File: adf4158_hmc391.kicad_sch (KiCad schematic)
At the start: 48 parts, among them U4 HMC391, U5 AD8065, U6 ADF4158, Y1 KT2016K

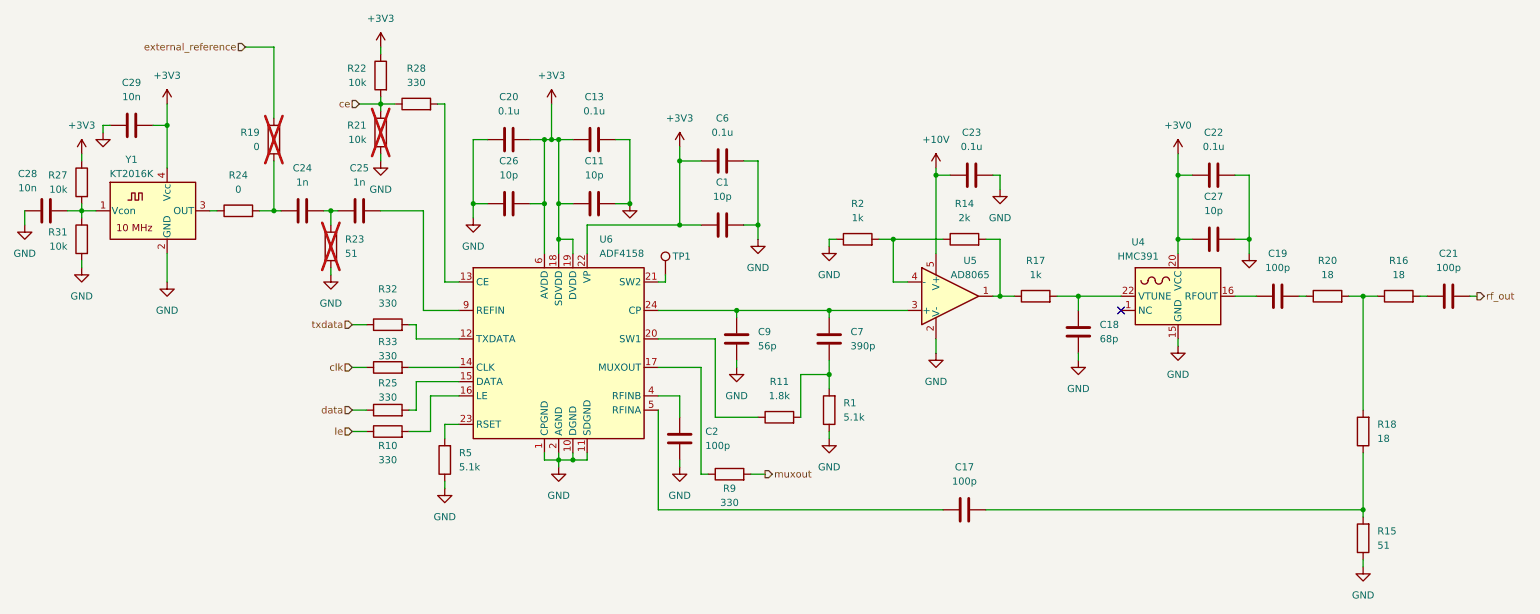
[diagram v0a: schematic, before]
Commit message: switch to 4-layer 1.6mm PCB stackup from JLCPCB
- By recommendation of reviewers, use a 4-layer 1.6 PCB stackup from
JLCPCB that gives 0.6 mm 50 ohm CPWG traces on the top layer.

- Use an SMA connector with a thin pin for the RF output.

- Remove 51 ohm resistor loading the ADF4518 PCB. This is believed
to be a mistake in the evaluation board schematic.

- Add M2 mounting holes to the board corners.

- Connect NC pins of HMC391 to GND as in the evaluation board.

Signed-off-by: Daniel Estévez <daniel@destevez.net>
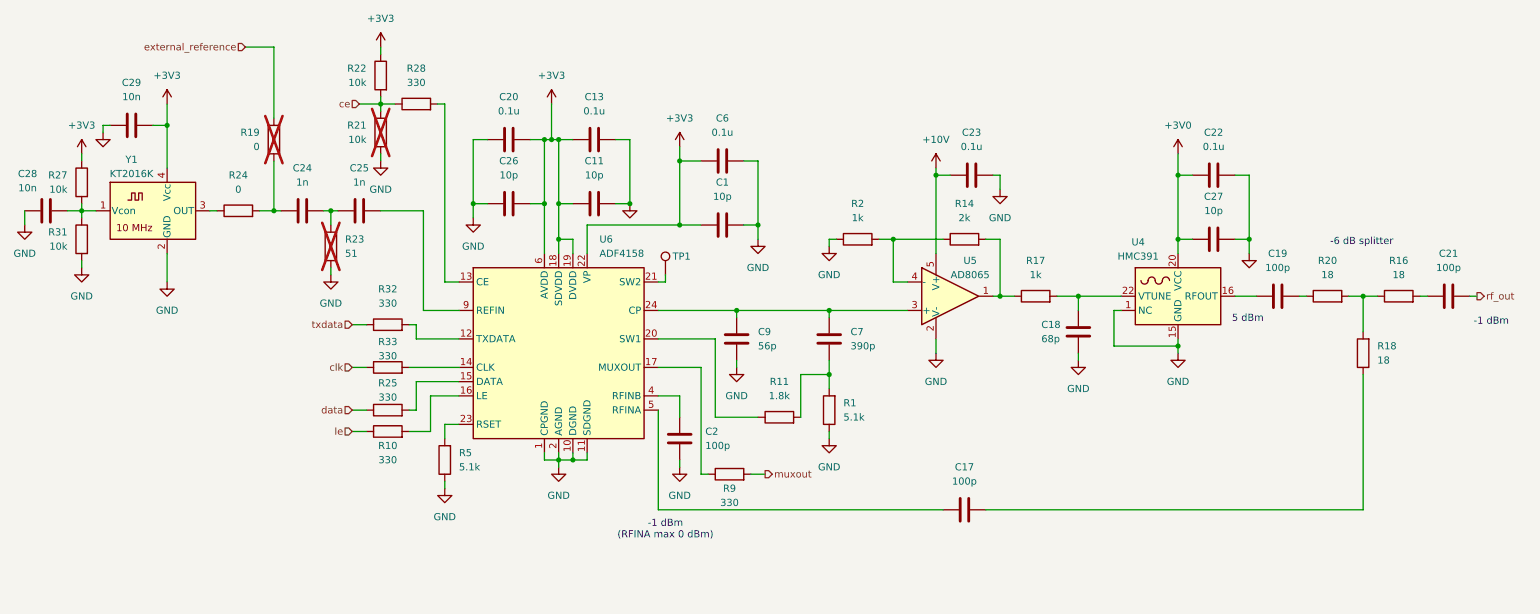
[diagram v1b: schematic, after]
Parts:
- removed R15: 51, Resistor_SMD:R_0402_1005Metric, symbol Device:R
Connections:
- net GND: now also U4.1 (NC), U4.10 (NC), U4.11 (NC), U4.12 (NC), U4.13 (NC), U4.14 (NC), U4.17 (NC), U4.18 (NC), U4.19 (NC), U4.2 (NC), U4.21 (NC), U4.23 (NC), U4.24 (NC), U4.3 (NC), U4.4 (NC), U4.5 (NC), U4.6 (NC), U4.7 (NC), U4.8 (NC), U4.9 (NC)
- no-connect marks 1 -> 0
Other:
- note added: "-1 dBm"
- note added: "-1 dBm (RFINA max 0 dBm)"
- note added: "-6 dB splitter"
- note added: "5 dBm"
- moved on the sheet: R18
